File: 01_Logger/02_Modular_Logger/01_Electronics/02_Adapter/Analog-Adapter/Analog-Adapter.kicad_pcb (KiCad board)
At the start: 4 copper layers, 74.2 x 32.2 mm, 34 parts, among them IC201 MSP430FR2673, IC301 TXB0104PW, K301 SSM3K127TU, SW201 SKRKAEE020, SW202 A6H-8101, X201 ESQ-104-14-G-D, X202 Conn_02x03_Counter_Clockwise, X203 Conn_01x03, X301 Molex Nano-Fit 105314-1*114, Y201 9HT11-32.768KDZF-T

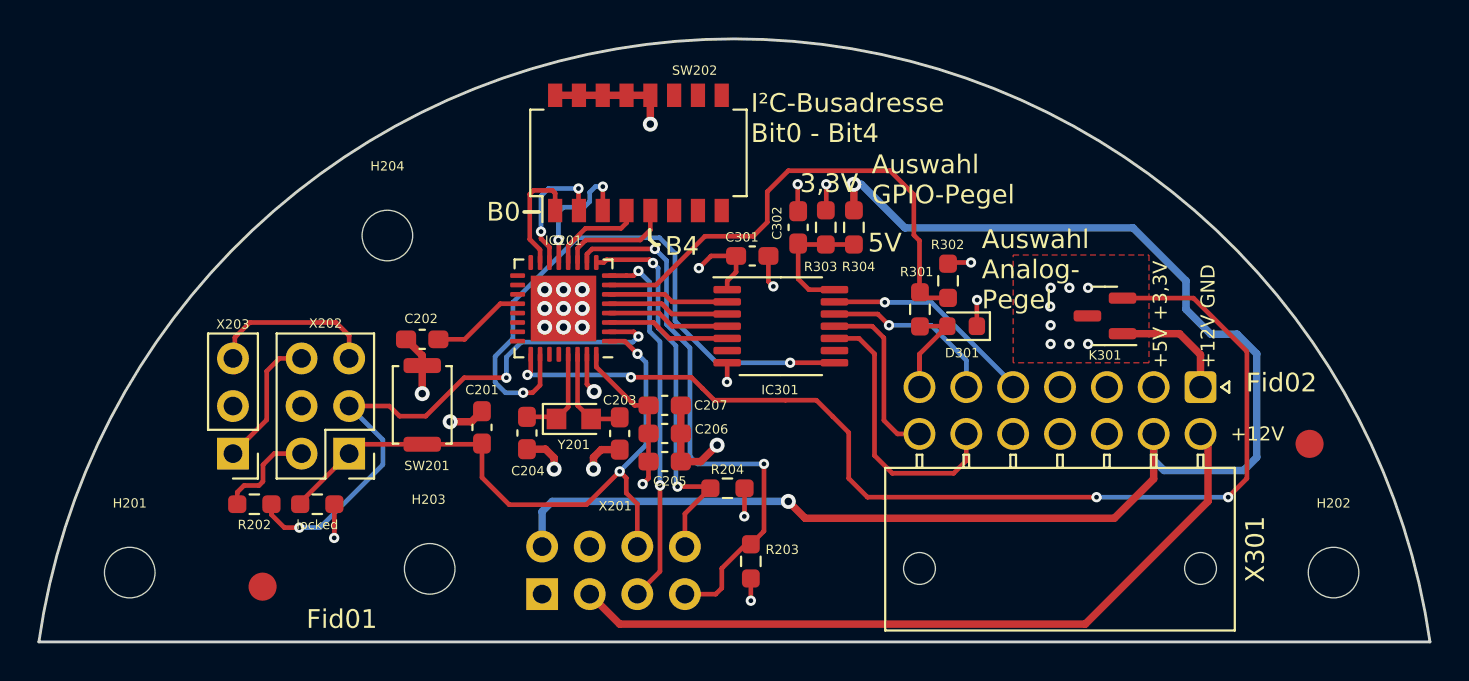
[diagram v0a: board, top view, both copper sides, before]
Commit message: Analog-Interfaceboard V0.2
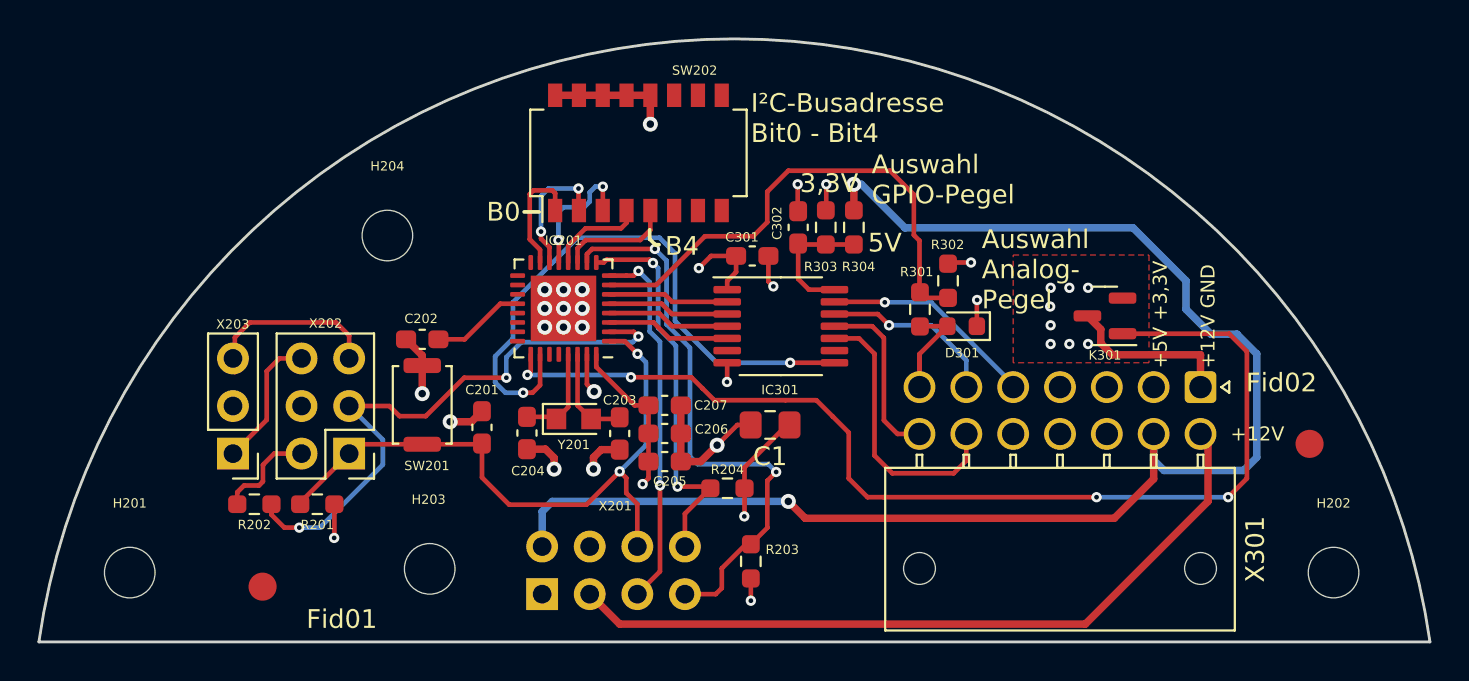
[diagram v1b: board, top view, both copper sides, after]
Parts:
- added C1: 100uF, Capacitor_SMD:C_0805_2012Metric_Pad1.18x1.45mm_HandSolder, F.Cu at (139.0, 53.1)
- C201: value 1nF -> 1nF 6,3V
- C205: value 100nF -> 100nF 6,3V
- C206: value 1µF -> 1µF, <200m ESR
- C207: value 4,7µF -> 4,7µF 6,3V
- R304: value 0 -> 0R
- Y201: value 9HT11-32.768KDZF-T -> 9HT11-32.768KDZF-T
- renumbered locked to R201
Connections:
- K301 pad 1: Net-(X301-Pad1) -> /MCU/Sensor_Lowside_Switch
- K301 pad 2: /MCU/Sensor_Lowside_Switch -> GND
- K301 pad 3: GND -> Net-(X301-Pin_1)
- X301 pad 1: Net-(X301-Pad1) -> Net-(X301-Pin_1)
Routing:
- net Net-(X301-Pin_1): track 0.00 -> 9.54 mm
- net Net-(X301-Pad1): track 6.35 -> 0.00 mm
- net +3V3: track 18.8 -> 23.2 mm
- net GND: track 31.1 -> 32.8 mm
- net /MCU/Sensor_Lowside_Switch: track 58.7 -> 57.9 mm
- net /MCU/UCB0_SCL: track 30.0 -> 30.6 mm
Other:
- board text added: "HyFiVe Analog-Interfaceboard V0.2 11/2025"
- board text removed: "HyFiVe Analog-Interfaceboard V0.1 12/2022"
